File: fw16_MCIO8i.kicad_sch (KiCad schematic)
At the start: 35 parts, among them J1 FXBeam, J2 Fan0, J3 Fan1, J4 173162-0131, U1 BR24G32FVT-3GE2

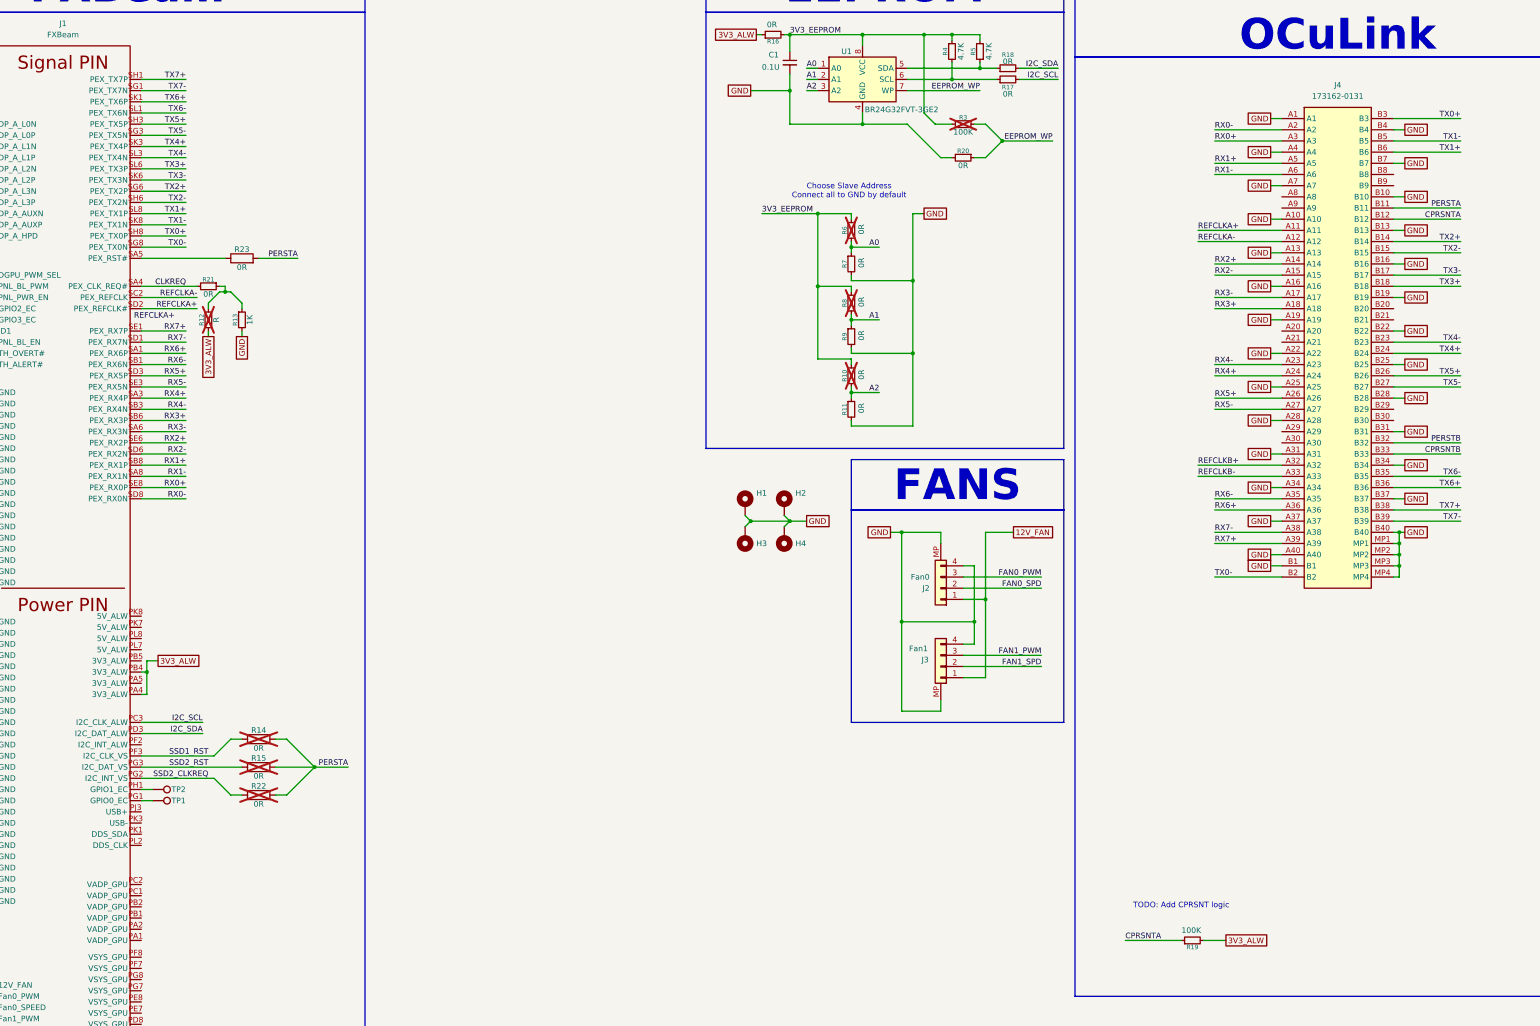
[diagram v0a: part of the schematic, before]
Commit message: Connected MCIO on Schematics
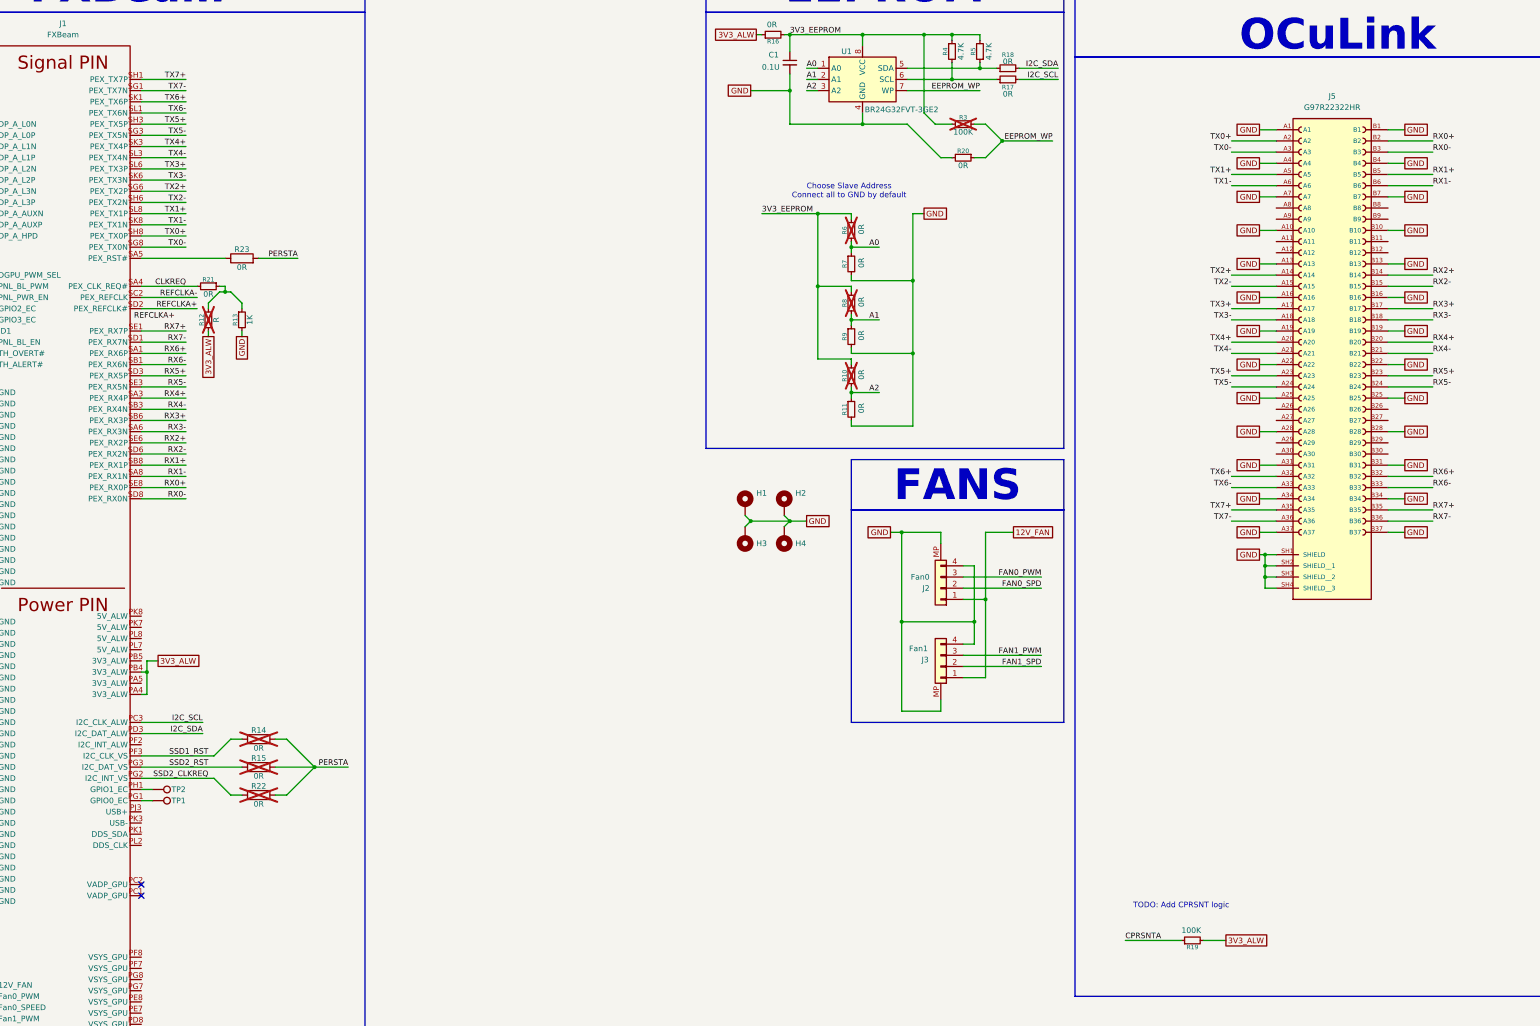
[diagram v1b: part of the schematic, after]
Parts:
- removed J4: 173162-0131, Nano_Pitch:Nano-Pitch-173162-0131_JLC-DRC, symbol Nano_Pitch:173162-0131
- added J5: G97R22322HR, MCIO-connector:AMPHENOL_G97R22322HR, symbol MCIO_Connector:G97R22322HR
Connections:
- net GND: now also J5.A1, J5.A10, J5.A13, J5.A16, J5.A19, J5.A22, J5.A25, J5.A28, J5.A31, J5.A34, J5.A37, J5.A4, J5.A7, J5.B1, J5.B10, J5.B13, J5.B16, J5.B19, J5.B22, J5.B25, J5.B28, J5.B31, J5.B34, J5.B37, J5.B4, J5.B7, J5.SH1 (SHIELD), J5.SH2 (SHIELD__1), J5.SH3 (SHIELD__2), J5.SH4 (SHIELD__3)
- net RX0+: now also J5.B2
- net RX0-: now also J5.B3
- net RX1+: now also J5.B5
- net RX1-: now also J5.B6
- net RX2+: now also J5.B14
- net RX2-: now also J5.B15
- net RX3+: now also J5.B17
- net RX3-: now also J5.B18
- net RX4+: now also J5.B20
- net RX4-: now also J5.B21
- net RX5+: now also J5.B23
- net RX5-: now also J5.B24
- net RX6+: now also J5.B32
- net RX6-: now also J5.B33
- net RX7+: now also J5.B35
- net RX7-: now also J5.B36
- net TX0+: now also J5.A2
- net TX0-: now also J5.A3
- net TX1+: now also J5.A5
- net TX1-: now also J5.A6
- net TX2+: now also J5.A14
- net TX2-: now also J5.A15
- net TX3+: now also J5.A17
- net TX3-: now also J5.A18
- net TX4+: now also J5.A20
- net TX4-: now also J5.A21
- net TX5+: now also J5.A23
- net TX5-: now also J5.A24
- net TX6+: now also J5.A32
- net TX6-: now also J5.A33
- net TX7+: now also J5.A35
- net TX7-: now also J5.A36
- no-connect marks 0 -> 2

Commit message: Changed naming to lowercase
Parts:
- C1: value 0.1U -> C_Small; footprint Capacitor_SMD:C_0402_1005Metric -> (none)
- H1, H2, H3, H4: footprint Expansion_Bay:MountingHole_6.2mm -> (none)
- J1: symbol Expansion_Bay:FXBeam -> expansion_bay:FXBeam; now in the parts list
- J2: value Fan0 -> Conn_01x04; footprint fpc-fan:JUSHUO_AFC05-S04FIA-00 -> (none); Part Nr. JUSHUO AFC05-S04FIA-00 -> (none)
- J3: value Fan1 -> Conn_01x04; footprint fpc-fan:JUSHUO_AFC05-S04FIA-00 -> (none); Part Nr. JUSHUO AFC05-S04FIA-00 -> (none)
- R1, R2: value 330K -> R; footprint Resistor_SMD:R_0402_1005Metric -> (none); Tolerance 1% -> (none)
- R10, R11, R16, R17, R18, R20, R21, R6, R7, R8, R9: value 0R -> R_Small; footprint Resistor_SMD:R_0402_1005Metric -> (none)
- R12: value R -> R_Small; footprint Resistor_SMD:R_0402_1005Metric -> (none)
- R13: value 1K -> R_Small; footprint Resistor_SMD:R_0402_1005Metric -> (none)
- R14, R15, R22, R23: value 0R -> R; footprint Resistor_SMD:R_0402_1005Metric -> (none)
- R19: value 100K -> R_Small; footprint Resistor_SMD:R_0402_1005Metric -> (none)
- R3: value 100K -> R_Small; footprint Resistor_SMD:R_0402_1005Metric -> (none); Tolerance 1% -> (none)
- R4, R5: value 4.7K -> R_Small; footprint Resistor_SMD:R_0402_1005Metric -> (none); Tolerance 1% -> (none)
- TP1, TP2: footprint TestPoint:TestPoint_Pad_D1.0mm -> (none)
- U1: value BR24G32FVT-3GE2 -> CAT24C256; footprint Package_SO:TSSOP-8_4.4x3mm_P0.65mm -> (none)
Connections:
- net GND: no longer J2.MP, J3.MP
- no-connect marks 2 -> 18

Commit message: New fan connector
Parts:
- FAN_L1: renamed from J2; value Conn_01x04 -> FAN; footprint (none) -> fan-connector:AMPHENOL_59453-041110EDHLF; symbol Connector_Generic:Conn_01x04 -> fan-connector:59453-041110EDHLF; MANUFACTURER (none) -> Amphenol; MAXIMUM_PACKAGE_HEIGHT (none) -> 3.00mm; PARTREV (none) -> D; STANDARD (none) -> Manufacturer Recommendations
- FAN_R1: renamed from J3; value Conn_01x04 -> FAN; footprint (none) -> fan-connector:AMPHENOL_59453-041110EDHLF; symbol Connector_Generic:Conn_01x04 -> fan-connector:59453-041110EDHLF; MANUFACTURER (none) -> Amphenol; MAXIMUM_PACKAGE_HEIGHT (none) -> 3.00mm; PARTREV (none) -> D; STANDARD (none) -> Manufacturer Recommendations
- FXBeam1: renamed from J1; value FXBeam -> IN; footprint Expansion_Bay:FXBeam -> expansion_bay:FXBeam
- MCIO1: renamed from J5; footprint MCIO-connector:AMPHENOL_G97R22322HR -> mcio-connector:AMPHENOL_G97R22322HR; symbol MCIO_Connector:G97R22322HR -> mcio-connector:G97R22322HR
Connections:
- net 3V3_ALW: now also FXBeam1.PA5 (3V3_ALW), FXBeam1.PB5 (3V3_ALW)
- net GND: now also MCIO1.GND (A7); no longer MCIO1.A7
- net 5V_ALW: now reaches FXBeam1.PK7 (5V_ALW)
- net 5V_ALW: now also FXBeam1.PK8 (5V_ALW), FXBeam1.PL7 (5V_ALW), FXBeam1.PL8 (5V_ALW)
- no-connect marks 18 -> 59
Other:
- moved on the sheet: FAN_L1, FAN_R1

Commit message: Cleanup
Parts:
- removed C1: C_Small, symbol Device:C_Small
- removed R1, R14, R15, R2, R22, R23: R, symbol Device:R
- removed R10, R11, R12, R13, R16, R17, R18, R19, R20, R21, R3, R4, R5, R6, R7, R8, R9: R_Small, symbol Device:R_Small
- removed TP1, TP2: TestPoint, symbol Connector:TestPoint
- removed U1: CAT24C256, symbol Memory_EEPROM:CAT24C256
- added C1: 0.1uF, PCM_JLCPCB:C_0402, symbol PCM_JLCPCB-Capacitors:0402,1uF
- added R1, R2: 330, PCM_JLCPCB:R_0402, symbol PCM_JLCPCB-Resistors:0402,330kΩ
- added R3, R50, R51: 10K, PCM_JLCPCB:R_0402, symbol PCM_JLCPCB-Resistors:0402,10kΩ
- added R4: 100k, PCM_JLCPCB:R_0402, symbol PCM_JLCPCB-Resistors:0402,100kΩ
- added TP3, TP5: TestPoint_Small, TestPoint:TestPoint_Pad_D1.0mm, symbol Connector:TestPoint_Small
- added U1: M24C32-FDW6TP, eeprom:TSSOP8_4P5X3P1X0P65_STM, symbol eeprom:M24C32-FDW6TP
- FAN_L1, FAN_R1: LCSC PN (none) -> C3168663
- H1, H2, H3, H4: footprint (none) -> expansion_bay:MountingHole_6.2mm
- MCIO1: LCSC Part (none) -> C5433519
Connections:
- net 3V3_ALW: now also C1.1, R3.1, R50.1, R51.1, U1.8 (VCC)
- net GND: now also MCIO1.A7 (GND), C1.2, R1.1, R2.1, R4.1, U1.1 (E0), U1.2 (E1), U1.3 (E2), U1.4 (VSS); no longer MCIO1.GND (A7)
- net I2C_SCL: now also R50.2, U1.6 (SCL)
- net I2C_SDA: now also R51.2, U1.5 (SDA)
- net at FXBeam1.PJ1 (ID0): now also R1.2, TP5.1
- net at FXBeam1.SL2 (ID1): now also R2.2, TP3.1
- net CLKREQ: no longer names the net of FXBeam1.SA4 (PEX_CLK_REQ#)
- net REFCLKA+: no longer names the net of FXBeam1.SD2 (PEX_REFCLK#)
- net REFCLKA-: no longer names the net of FXBeam1.SC2 (PEX_REFCLK)
- net SSD1_RST: no longer names the net of FXBeam1.PF3 (I2C_CLK_VS)
- net SSD2_CLKREQ: no longer names the net of FXBeam1.PG2 (I2C_INT_VS)
- net SSD2_RST: no longer names the net of FXBeam1.PG3 (I2C_DAT_VS)
- new net: R3.2, R4.2, U1.7 (WC)
- no-connect marks 59 -> 51
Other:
- note removed: "Choose Slave Address Connect all to GND by default"
- note removed: "TODO: Add CPRSNT logic"
- moved on the sheet: FAN_L1, FAN_R1, H1, H2, H3, H4

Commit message: Fixups
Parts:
- C1: value 0.1uF -> 1uF; PROD_ID CAP-25565 -> (none); Voltage 16V -> (none)
- FAN_L1, FAN_R1: value FAN -> 59453-041110EDHLF; LCSC PN C3168663 -> (none)
- FXBEAM1: renamed from FXBeam1; now left out of the parts list
- MCIO1: value G97R22322HR -> G97R22312HR; footprint mcio-connector:AMPHENOL_G97R22322HR -> mcio-connector:AMPHENOL_G97R22312HR; symbol mcio-connector:G97R22322HR -> mcio-connector:G97R22312HR; LCSC Part C5433519 -> (none); MPN (none) -> G97R22312HR
- R1, R2: value 330 -> 330kΩ; PROD_ID RES-15407 -> (none)
- R3, R50, R51: value 10K -> 10kΩ; PROD_ID RES-25567 -> (none)
- R4: value 100k -> 100kΩ; PROD_ID RES-25013 -> (none)
- TP3, TP5: footprint TestPoint:TestPoint_Pad_D1.0mm -> TestPoint:TestPoint_Pad_D3.0mm
- U1: now left out of the parts list
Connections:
- net RX0+: now also MCIO1.A2 (PER0+); no longer MCIO1.B2 (RX0+)
- net RX0-: now also MCIO1.A3 (PER0+); no longer MCIO1.B3 (RX0-)
- net RX1+: now also MCIO1.A5 (PER1+); no longer MCIO1.B5 (RX1+)
- net RX1-: now also MCIO1.A6 (PER1-); no longer MCIO1.B6 (RX1-)
- net RX2+: now also MCIO1.A14 (PER2+); no longer MCIO1.B14 (RX2+)
- net RX2-: now also MCIO1.A15 (PER2-); no longer MCIO1.B15 (RX2-)
- net RX3+: now also MCIO1.A17 (PER3+); no longer MCIO1.B17 (RX3+)
- net RX3-: now also MCIO1.A18 (PER3-); no longer MCIO1.B18 (RX3-)
- net RX4+: now also MCIO1.A20 (PER4+); no longer MCIO1.B20 (RX4+)
- net RX4-: now also MCIO1.A21 (PER4-); no longer MCIO1.B21 (RX4-)
- net RX5+: now also MCIO1.A23 (PER5+); no longer MCIO1.B23 (RX5+)
- net RX5-: now also MCIO1.A24 (PER5-); no longer MCIO1.B24 (RX5-)
- net RX6+: now also MCIO1.A32 (PER6+); no longer MCIO1.B32 (RX6+)
- net RX6-: now also MCIO1.A33 (PER6-); no longer MCIO1.B33 (RX6-)
- net RX7+: now also MCIO1.A35 (PER7+); no longer MCIO1.B35 (RX7+)
- net RX7-: now also MCIO1.A36 (PER7+); no longer MCIO1.B36 (RX7-)
- net TX0+: now also MCIO1.B2 (PET0+); no longer MCIO1.A2 (TX0+)
- net TX0-: now also MCIO1.B3 (PET0-); no longer MCIO1.A3 (TX0-)
- net TX1+: now also MCIO1.B5 (PET1+); no longer MCIO1.A5 (TX1+)
- net TX1-: now also MCIO1.B6 (PET1-); no longer MCIO1.A6 (TX1-)
- net TX2+: now also MCIO1.B14 (PET2+); no longer MCIO1.A14 (TX2+)
- net TX2-: now also MCIO1.B15 (PET2-); no longer MCIO1.A15 (TX2-)
- net TX3+: now also MCIO1.B17 (PET3+); no longer MCIO1.A17 (TX3+)
- net TX3-: now also MCIO1.B18 (PET3-); no longer MCIO1.A18 (TX3-)
- net TX4+: now also MCIO1.B20 (PET4+); no longer MCIO1.A20 (TX4+)
- net TX4-: now also MCIO1.B21 (PET4-); no longer MCIO1.A21 (TX4-)
- net TX5+: now also MCIO1.B23 (PET5+); no longer MCIO1.A23 (TX5+)
- net TX5-: now also MCIO1.B24 (PET5-); no longer MCIO1.A24 (TX5-)
- net TX6+: now also MCIO1.B32 (PET6+); no longer MCIO1.A32 (TX6+)
- net TX6-: now also MCIO1.B33 (PET6-); no longer MCIO1.A33 (TX6-)
- net TX7+: now also MCIO1.B35 (PET7+); no longer MCIO1.A35 (TX7+)
- net TX7-: now also MCIO1.B36 (PET7-); no longer MCIO1.A36 (TX7-)
- net PEX_RST: now reaches FXBEAM1.SA5 (PEX_RST#)
- net PEX_RST: now also MCIO1.B11 (PERST)
- net PEX_CLK+: now reaches FXBEAM1.SC2 (PEX_REFCLK)
- net PEX_CLK+: now also MCIO1.A11 (REFCLK_A+)
- net PEX_CLK-: now reaches FXBEAM1.SD2 (PEX_REFCLK-)
- net PEX_CLK-: now also MCIO1.A12 (REFCLK_A-)

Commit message: Fox
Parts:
- renumbered U1 to EEPROM1

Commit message: cat
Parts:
- removed H1, H2, H3, H4: MountingHole_Pad, expansion_bay:MountingHole_6.2mm, symbol Mechanical:MountingHole_Pad
- removed R3: 10kΩ, PCM_JLCPCB:R_0402, symbol PCM_JLCPCB-Resistors:0402,10kΩ
- removed R4: 100kΩ, PCM_JLCPCB:R_0402, symbol PCM_JLCPCB-Resistors:0402,100kΩ
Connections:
- net GND: now also EEPROM1.7 (WC)
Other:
- moved on the sheet: FAN_L1, FAN_R1

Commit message: changed parts
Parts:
- FAN_L1, FAN_R1: value 59453-041110EDHLF -> F3011B7H111005E200; footprint fan-connector:AMPHENOL_59453-041110EDHLF -> fan-connector:AMPHENOL_F33D-1A7H1-E7C04; symbol fan-connector:59453-041110EDHLF -> fan-connector:F33D-1A7H1-E7C04; MAXIMUM_PACKAGE_HEIGHT 3.00mm -> 2.4mm; MPN (none) -> 609-F33D-1A7H1-E7C04CT-ND; PARTREV D -> B
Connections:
- net 12V_FAN: now also FAN_L1.4, FAN_R1.4; no longer FAN_L1.1, FAN_R1.1
- net FAN0_PWM: now also FAN_L1.2; no longer FAN_L1.3
- net FAN0_SPD: now also FAN_L1.3; no longer FAN_L1.2
- net FAN1_PWM: now also FAN_R1.2; no longer FAN_R1.3
- net FAN1_SPD: now also FAN_R1.3; no longer FAN_R1.2
- net GND: now also FAN_L1.1, FAN_L1.SH1, FAN_L1.SH2, FAN_R1.1, FAN_R1.SH1, FAN_R1.SH2; no longer FAN_L1.4, FAN_R1.4
- net I2C_SCL: now also FXBEAM1.PF2 (I2C_INT_ALW); no longer FXBEAM1.PC3 (I2C_CLK_ALW)
- net PE_SDA: now reaches FXBEAM1.PG2 (I2C_INT_VS)
- net PE_SDA: now also MCIO1.B9 (SM_SDA)
- net PE_SCL: now reaches FXBEAM1.PG3 (I2C_DAT_VS)
- net PE_SCL: now also MCIO1.B8 (SM_SCL)
- no-connect marks 51 -> 4
